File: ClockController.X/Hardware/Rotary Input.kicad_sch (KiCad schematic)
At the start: 7 parts

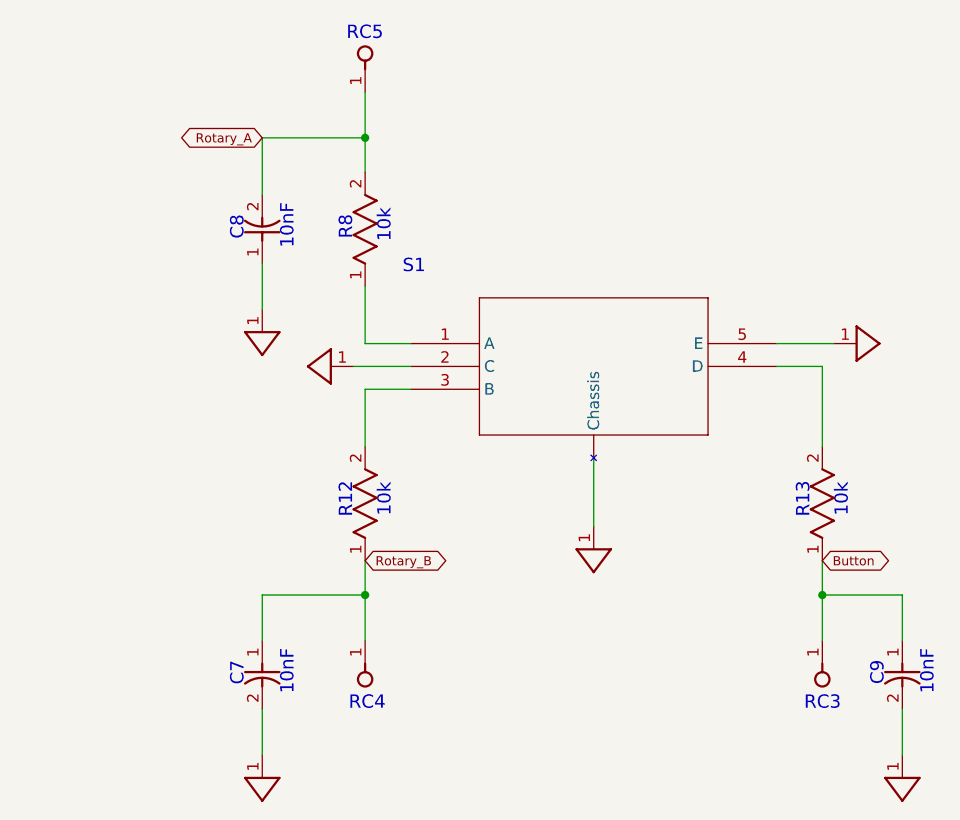
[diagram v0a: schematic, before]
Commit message: Replace the imported objects with native kicad equivalents
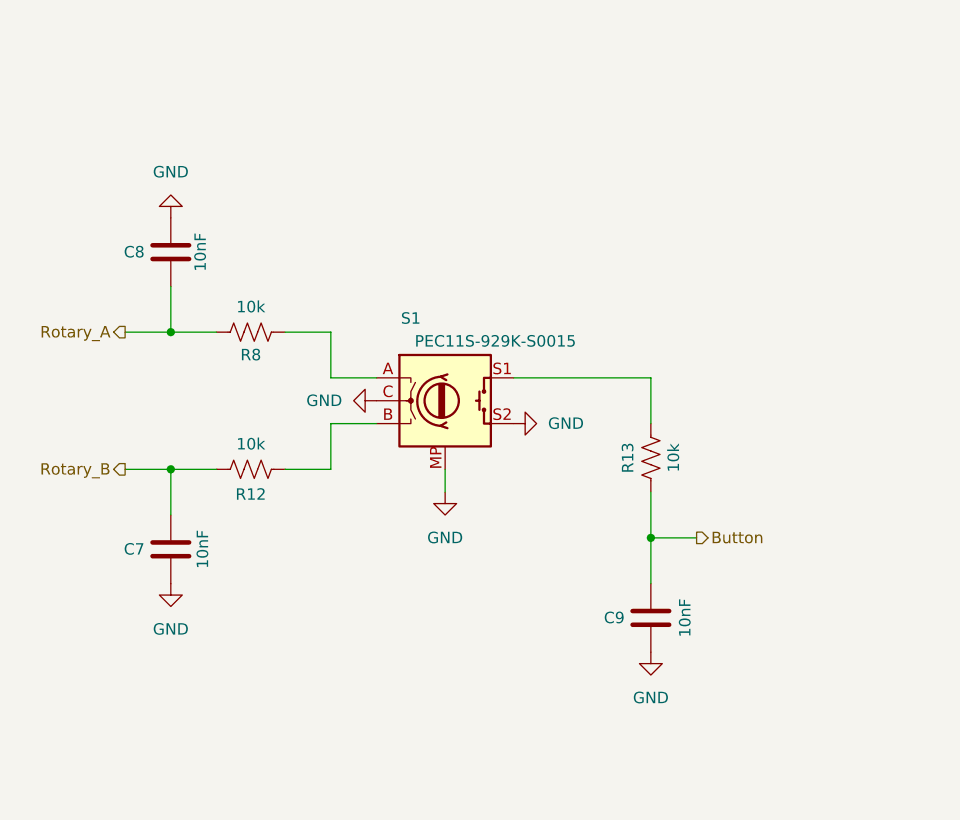
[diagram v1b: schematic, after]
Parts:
- C7, C8, C9: symbol Clock Controller-eagle-import:CAP_0603 -> Device:C
- R12, R13, R8: symbol Clock Controller-eagle-import:RES_0603 -> Device:R_US
- S1: footprint Clock Controller:IC5_PEC11S-929K-S0015_BRN -> Rotary_Encoder_:PEC11S-929K-S0015; symbol Clock Controller-eagle-import:PEC11S-929K-S0015 -> Device:RotaryEncoder_Switch_MP
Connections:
- net at R8.1: now also S1.A; no longer S1.1 (A)
- net Rotary_B: now reaches R12.2
- net Rotary_B: now also C7.2; no longer S1.3 (B)
- net at R13.2: now also S1.S1; no longer S1.4 (D)
- removed net GND_DIGITAL: C7.2, C8.1, C9.2, S1.10 (Chassis), S1.2 (C), S1.5 (E), S1.6 (Chassis)
- net RC3 renamed Button
- net RC4: no longer names the net of R12.1
- net RC4: now also S1.B; no longer C7.1
- net RC5 renamed Rotary_A
- new net GND: C7.1, C8.1, C9.2, S1.C, S1.MP, S1.S2
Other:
- note removed: "10k"
- note removed: "10nF"
- note removed: "C7"
- note removed: "C8"
- note removed: "C9"
- note removed: "R12"
- note removed: "R13"
- note removed: "R8"
- note removed: "RC3"
- note removed: "RC4"
- note removed: "RC5"
- note removed: "S1"

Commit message: Named all nets
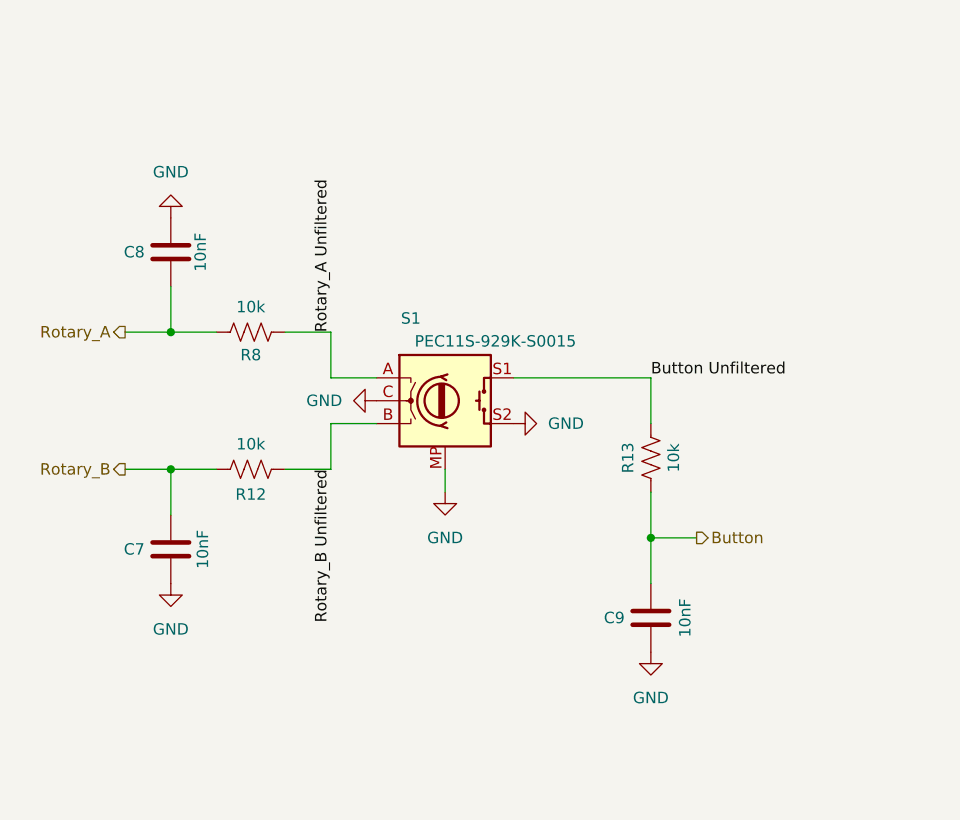
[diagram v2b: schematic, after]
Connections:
- net Rotary_A Unfiltered: now reaches R8.1, S1.A
- net Rotary_B Unfiltered: now reaches R12.1, S1.B
- net Button Unfiltered: now reaches R13.2, S1.S1
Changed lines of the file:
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@@
+		)
+	)
+	(label "Rotary_A Unfiltered"
+		(at 119.38 93.98 90)
+		(effects
+			(font
+				(size 1.27 1.27)
+			)
+			(justify left bottom)
+		)
+	)
+	(label "Rotary_B Unfiltered"
+		(at 119.38 109.22 270)
+		(effects
+			(font
+				(size 1.27 1.27)
+			)
+			(justify right bottom)
+		)
+	)
+	(label "Button Unfiltered"
+		(at 154.94 99.06 0)
+		(effects
+			(font
+				(size 1.27 1.27)
+			)
+			(justify left bottom)
 		)
 	)
@@
 		)
 		(instances
-			(project ""
+			(project "Clock Controller"
 				(path "/de4049ea-1674-4dcc-86d3-bb1be3dcf2e7/867f44d7-ba62-42d8-959c-be37f05c9614"
 					(reference "#PWR023")
